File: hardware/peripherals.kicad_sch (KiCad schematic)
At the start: 32 parts, among them J1 USB_C_Receptacle_USB2.0_14P, J2 PCM12SMTR, J3 BM03B-SRSS-TB, Q1 2N7002, SW1 SW_Push, U1 USBLC6-2SC6, U2 74AHCT1G125, U4 74AHCT1G32, U5 DS3231MZ

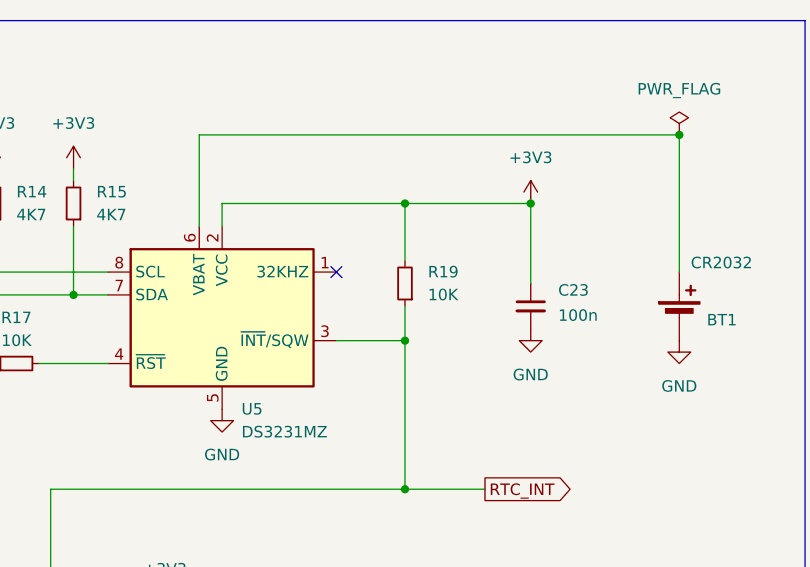
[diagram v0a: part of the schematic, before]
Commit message: workaround: mark R19 (RTC_INT pull-up) as DNP
R19 pulls Q1 gate high at power-on, preventing CM4 boot by
holding GLOBAL_EN low. Mark as DNP until the wake circuit is
redesigned (see #31).
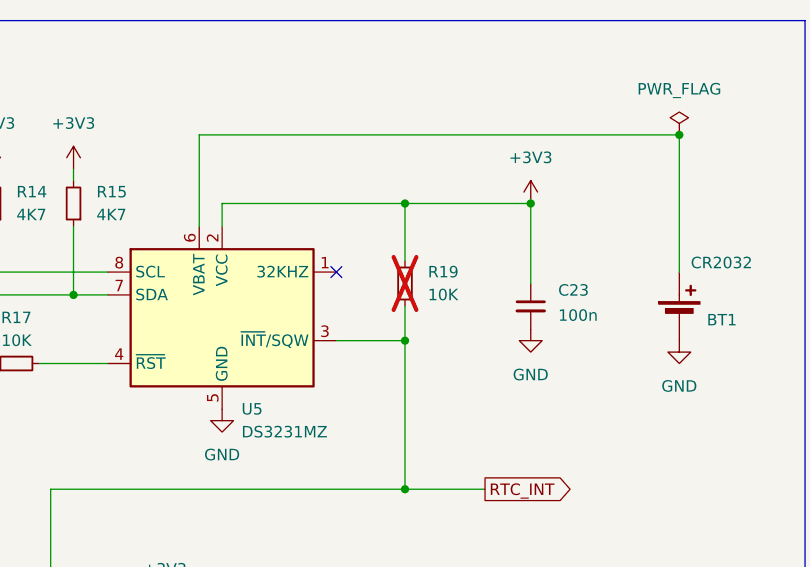
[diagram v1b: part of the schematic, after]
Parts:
- R19: now not fitted
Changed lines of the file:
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@@
 		(on_board yes)
 		(in_pos_files yes)
-		(dnp no)
+		(dnp yes)
 		(fields_autoplaced yes)
 		(property "Reference" "R19"
